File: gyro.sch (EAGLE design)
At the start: 12 parts, among them IC3 FXAS21002C

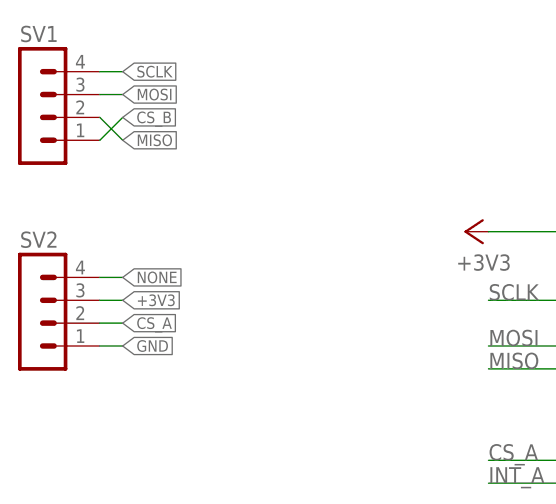
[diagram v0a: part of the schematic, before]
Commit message: INT_A i dopasowanie goldpinow
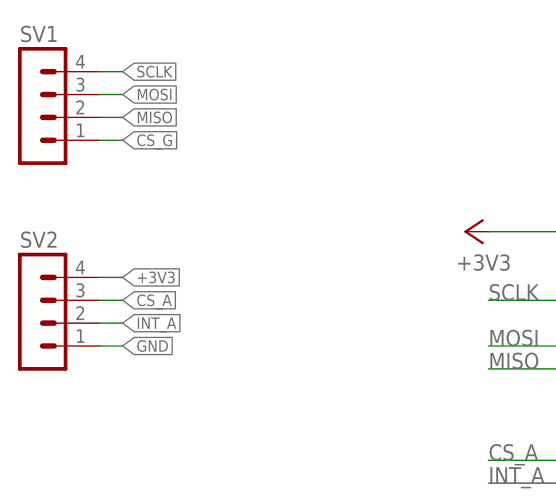
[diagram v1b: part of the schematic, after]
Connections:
- net CS_B renamed CS_G
- net N$28 renamed INT_G
- removed net NONE: SV2.4
- net +3V3: now also SV2.4; no longer SV2.3
- net CS_A: now also SV2.3; no longer SV2.2
- net INT_A: now also SV2.2
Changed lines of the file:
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@@
 <segment>
 <pinref part="SV1" gate="1" pin="2"/>
-<wire x1="-96.52" y1="60.96" x2="-93.98" y2="58.42" width="0.1524" layer="91"/>
-<label x="-93.98" y="58.42" size="1.27" layer="95" xref="yes"/>
+<wire x1="-96.52" y1="60.96" x2="-93.98" y2="60.96" width="0.1524" layer="91"/>
+<label x="-93.98" y="60.96" size="1.27" layer="95" xref="yes"/>
 </segment>
 </net>
@@
 <label x="-53.34" y="20.32" size="1.778" layer="95"/>
 </segment>
+<segment>
+<pinref part="SV2" gate="1" pin="2"/>
+<wire x1="-96.52" y1="38.1" x2="-93.98" y2="38.1" width="0.1524" layer="91"/>
+<label x="-93.98" y="38.1" size="1.27" layer="95" xref="yes"/>
+</segment>
 </net>
 <net name="+3V3" class="0">
@@
 </segment>
 <segment>
-<pinref part="SV2" gate="1" pin="3"/>
-<wire x1="-96.52" y1="40.64" x2="-93.98" y2="40.64" width="0.1524" layer="91"/>
-<label x="-93.98" y="40.64" size="1.27" layer="95" xref="yes"/>
+<pinref part="SV2" gate="1" pin="4"/>
+<wire x1="-96.52" y1="43.18" x2="-93.98" y2="43.18" width="0.1524" layer="91"/>
+<label x="-93.98" y="43.18" size="1.27" layer="95" xref="yes"/>
 </segment>
 <segment>
@@
 </segment>
 </net>
-<net name="CS_B" class="0">
-<segment>
-<pinref part="IC3" gate="G$1" pin="SPI_CS_B"/>
-<wire x1="17.78" y1="-30.48" x2="20.32" y2="-30.48" width="0.1524" layer="91"/>
-</segment>
-<segment>
-<pinref part="SV1" gate="1" pin="1"/>
-<wire x1="-96.52" y1="58.42" x2="-93.98" y2="60.96" width="0.1524" layer="91"/>
-<label x="-93.98" y="60.96" size="1.27" layer="95" xref="yes"/>
-</segment>
-</net>
 <net name="N$26" class="0">
 <segment>
@@
 </segment>
 </net>
-<net name="N$28" class="0">
-<segment>
-<pinref part="IC3" gate="G$1" pin="INT1"/>
-<wire x1="-22.86" y1="-30.48" x2="-25.4" y2="-30.48" width="0.1524" layer="91"/>
-</segment>
-</net>
 <net name="N$30" class="0">
 <segment>
@@
 </segment>
 </net>
-<net name="NONE" class="0">
+<net name="INT_G" class="0">
 <segment>
-<pinref part="SV2" gate="1" pin="4"/>
-<wire x1="-96.52" y1="43.18" x2="-93.98" y2="43.18" width="0.1524" layer="91"/>
-<label x="-93.98" y="43.18" size="1.27" layer="95" xref="yes"/>
+<pinref part="IC3" gate="G$1" pin="INT1"/>
+<wire x1="-22.86" y1="-30.48" x2="-25.4" y2="-30.48" width="0.1524" layer="91"/>
 </segment>
 </net>
@@
 </segment>
 <segment>
-<pinref part="SV2" gate="1" pin="2"/>
-<wire x1="-96.52" y1="38.1" x2="-93.98" y2="38.1" width="0.1524" layer="91"/>
-<label x="-93.98" y="38.1" size="1.27" layer="95" xref="yes"/>
+<pinref part="SV2" gate="1" pin="3"/>
+<wire x1="-96.52" y1="40.64" x2="-93.98" y2="40.64" width="0.1524" layer="91"/>
+<label x="-93.98" y="40.64" size="1.27" layer="95" xref="yes"/>
 </segment>
 </net>
+<net name="CS_G" class="0">
+<segment>
+<pinref part="IC3" gate="G$1" pin="SPI_CS_B"/>
+<wire x1="17.78" y1="-30.48" x2="20.32" y2="-30.48" width="0.1524" layer="91"/>
+</segment>
+<segment>
+<pinref part="SV1" gate="1" pin="1"/>
+<wire x1="-96.52" y1="58.42" x2="-93.98" y2="58.42" width="0.1524" layer="91"/>
+<label x="-93.98" y="58.42" size="1.27" layer="95" xref="yes"/>
+</segment>
+</net>

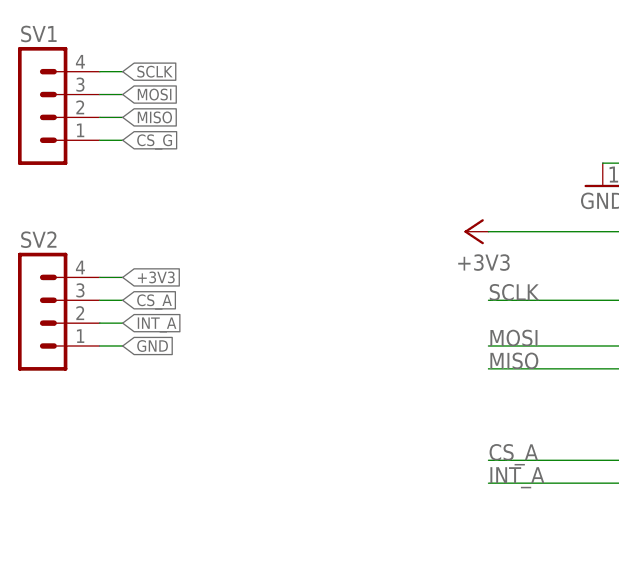
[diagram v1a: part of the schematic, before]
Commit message: dodanie wymiarowania do gyro i zepsucie termali :P
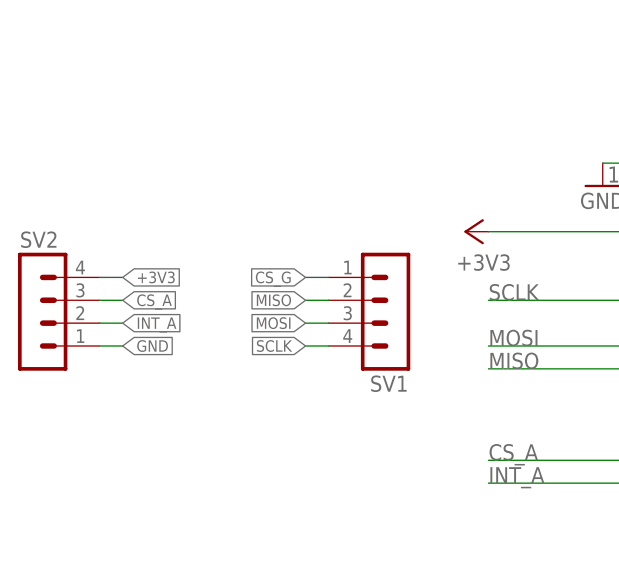
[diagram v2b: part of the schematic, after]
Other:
- moved on the sheet: SV1
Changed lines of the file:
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@@
 <instance part="C9" gate="G$1" x="30.48" y="-20.32"/>
 <instance part="C10" gate="G$1" x="35.56" y="-38.1"/>
-<instance part="SV1" gate="1" x="-104.14" y="63.5"/>
+<instance part="SV1" gate="1" x="-63.5" y="38.1" rot="R180"/>
 <instance part="SV2" gate="1" x="-104.14" y="40.64"/>
 <instance part="R1" gate="G$1" x="-43.18" y="-25.4" rot="R90"/>
@@
 <segment>
 <pinref part="SV1" gate="1" pin="3"/>
-<wire x1="-96.52" y1="63.5" x2="-93.98" y2="63.5" width="0.1524" layer="91"/>
-<label x="-93.98" y="63.5" size="1.27" layer="95" xref="yes"/>
+<wire x1="-71.12" y1="38.1" x2="-73.66" y2="38.1" width="0.1524" layer="91"/>
+<label x="-73.66" y="38.1" size="1.27" layer="95" rot="R180" xref="yes"/>
 </segment>
 </net>
@@
 <segment>
 <pinref part="SV1" gate="1" pin="2"/>
-<wire x1="-96.52" y1="60.96" x2="-93.98" y2="60.96" width="0.1524" layer="91"/>
-<label x="-93.98" y="60.96" size="1.27" layer="95" xref="yes"/>
+<wire x1="-71.12" y1="40.64" x2="-73.66" y2="40.64" width="0.1524" layer="91"/>
+<label x="-73.66" y="40.64" size="1.27" layer="95" rot="R180" xref="yes"/>
 </segment>
 </net>
@@
 <segment>
 <pinref part="SV1" gate="1" pin="4"/>
-<wire x1="-96.52" y1="66.04" x2="-93.98" y2="66.04" width="0.1524" layer="91"/>
-<label x="-93.98" y="66.04" size="1.27" layer="95" xref="yes"/>
+<wire x1="-71.12" y1="35.56" x2="-73.66" y2="35.56" width="0.1524" layer="91"/>
+<label x="-73.66" y="35.56" size="1.27" layer="95" rot="R180" xref="yes"/>
 </segment>
 </net>
@@
 <segment>
 <pinref part="SV1" gate="1" pin="1"/>
-<wire x1="-96.52" y1="58.42" x2="-93.98" y2="58.42" width="0.1524" layer="91"/>
-<label x="-93.98" y="58.42" size="1.27" layer="95" xref="yes"/>
-</segment>
-</net>
+<wire x1="-71.12" y1="43.18" x2="-73.66" y2="43.18" width="0.1524" layer="91"/>
+<label x="-73.66" y="43.18" size="1.27" layer="95" rot="R180" xref="yes"/>
+</segment>
+</net>

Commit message: gerbery do gyro
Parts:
- renumbered SV1 to SPI, SV2 to ZAS
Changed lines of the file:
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@@
 <part name="C9" library="rcl" deviceset="C-EU" device="C0603" value="100n"/>
 <part name="C10" library="rcl" deviceset="C-EU" device="C0603" value="100n"/>
-<part name="SV1" library="con-lstb" deviceset="MA04-1" device=""/>
-<part name="SV2" library="con-lstb" deviceset="MA04-1" device=""/>
+<part name="SPI" library="con-lstb" deviceset="MA04-1" device=""/>
+<part name="ZAS" library="con-lstb" deviceset="MA04-1" device=""/>
 <part name="R1" library="rcl" deviceset="R-EU_" device="R0603"/>
 <part name="+3V1" library="supply1" deviceset="+3V3" device=""/>
@@
 <instance part="C9" gate="G$1" x="30.48" y="-20.32"/>
 <instance part="C10" gate="G$1" x="35.56" y="-38.1"/>
-<instance part="SV1" gate="1" x="-63.5" y="38.1" rot="R180"/>
-<instance part="SV2" gate="1" x="-104.14" y="40.64"/>
+<instance part="SPI" gate="1" x="-63.5" y="38.1" rot="R180"/>
+<instance part="ZAS" gate="1" x="-104.14" y="40.64"/>
 <instance part="R1" gate="G$1" x="-43.18" y="-25.4" rot="R90"/>
 <instance part="+3V1" gate="G$1" x="-7.62" y="-60.96" rot="R180"/>
@@
 </segment>
 <segment>
-<pinref part="SV2" gate="1" pin="1"/>
+<pinref part="ZAS" gate="1" pin="1"/>
 <wire x1="-96.52" y1="35.56" x2="-93.98" y2="35.56" width="0.1524" layer="91"/>
 <label x="-93.98" y="35.56" size="1.27" layer="95" xref="yes"/>
@@
 </segment>
 <segment>
-<pinref part="SV1" gate="1" pin="3"/>
+<pinref part="SPI" gate="1" pin="3"/>
 <wire x1="-71.12" y1="38.1" x2="-73.66" y2="38.1" width="0.1524" layer="91"/>
 <label x="-73.66" y="38.1" size="1.27" layer="95" rot="R180" xref="yes"/>
@@
 </segment>
 <segment>
-<pinref part="SV1" gate="1" pin="2"/>
+<pinref part="SPI" gate="1" pin="2"/>
 <wire x1="-71.12" y1="40.64" x2="-73.66" y2="40.64" width="0.1524" layer="91"/>
 <label x="-73.66" y="40.64" size="1.27" layer="95" rot="R180" xref="yes"/>
@@
 </segment>
 <segment>
-<pinref part="SV1" gate="1" pin="4"/>
+<pinref part="SPI" gate="1" pin="4"/>
 <wire x1="-71.12" y1="35.56" x2="-73.66" y2="35.56" width="0.1524" layer="91"/>
 <label x="-73.66" y="35.56" size="1.27" layer="95" rot="R180" xref="yes"/>
@@
 </segment>
 <segment>
-<pinref part="SV2" gate="1" pin="2"/>
+<pinref part="ZAS" gate="1" pin="2"/>
 <wire x1="-96.52" y1="38.1" x2="-93.98" y2="38.1" width="0.1524" layer="91"/>
 <label x="-93.98" y="38.1" size="1.27" layer="95" xref="yes"/>
@@
 </segment>
 <segment>
-<pinref part="SV2" gate="1" pin="4"/>
+<pinref part="ZAS" gate="1" pin="4"/>
 <wire x1="-96.52" y1="43.18" x2="-93.98" y2="43.18" width="0.1524" layer="91"/>
 <label x="-93.98" y="43.18" size="1.27" layer="95" xref="yes"/>
@@
 </segment>
 <segment>
-<pinref part="SV2" gate="1" pin="3"/>
+<pinref part="ZAS" gate="1" pin="3"/>
 <wire x1="-96.52" y1="40.64" x2="-93.98" y2="40.64" width="0.1524" layer="91"/>
 <label x="-93.98" y="40.64" size="1.27" layer="95" xref="yes"/>
@@
 </segment>
 <segment>
-<pinref part="SV1" gate="1" pin="1"/>
+<pinref part="SPI" gate="1" pin="1"/>
 <wire x1="-71.12" y1="43.18" x2="-73.66" y2="43.18" width="0.1524" layer="91"/>
 <label x="-73.66" y="43.18" size="1.27" layer="95" rot="R180" xref="yes"/>

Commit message: poprawa bledow, dodanie rezystorow na wyjsciach stm-glownie w modolach, poprawa elementu 9axis z biblioteki
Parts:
- added INT_G: (no value), pinhead:PINHD-1X1
- added R2, R3, R4: (no value), rcl:R-EU_R0603
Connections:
- removed net INT_G: IC3.INT1
- new net N$1: R2.1, SPI.2
- new net N$2: INT_G.1, R3.2
- new net N$3: IC3.INT1, R3.1
- new net N$4: R4.2, ZAS.2
- net INT_A: now also R4.1; no longer ZAS.2
- net MISO: now also R2.2; no longer SPI.2
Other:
- moved on the sheet: ZAS
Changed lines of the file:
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@@
 <part name="R1" library="rcl" deviceset="R-EU_" device="R0603"/>
 <part name="+3V1" library="supply1" deviceset="+3V3" device=""/>
+<part name="INT_G" library="pinhead" deviceset="PINHD-1X1" device=""/>
+<part name="R2" library="rcl" deviceset="R-EU_" device="R0603"/>
+<part name="R3" library="rcl" deviceset="R-EU_" device="R0603"/>
+<part name="R4" library="rcl" deviceset="R-EU_" device="R0603"/>
 </parts>
 <sheets>
@@
 <instance part="C10" gate="G$1" x="35.56" y="-38.1"/>
 <instance part="SPI" gate="1" x="-63.5" y="38.1" rot="R180"/>
-<instance part="ZAS" gate="1" x="-104.14" y="40.64"/>
+<instance part="ZAS" gate="1" x="-116.84" y="40.64"/>
 <instance part="R1" gate="G$1" x="-43.18" y="-25.4" rot="R90"/>
 <instance part="+3V1" gate="G$1" x="-7.62" y="-60.96" rot="R180"/>
+<instance part="INT_G" gate="G$1" x="-66.04" y="-30.48" rot="R180"/>
+<instance part="R2" gate="G$1" x="-76.2" y="40.64" rot="R180"/>
+<instance part="R3" gate="G$1" x="-53.34" y="-30.48" rot="R180"/>
+<instance part="R4" gate="G$1" x="-104.14" y="38.1" rot="R180"/>
 </instances>
 <busses>
@@
 <segment>
 <pinref part="ZAS" gate="1" pin="1"/>
-<wire x1="-96.52" y1="35.56" x2="-93.98" y2="35.56" width="0.1524" layer="91"/>
-<label x="-93.98" y="35.56" size="1.27" layer="95" xref="yes"/>
+<wire x1="-109.22" y1="35.56" x2="-106.68" y2="35.56" width="0.1524" layer="91"/>
+<label x="-106.68" y="35.56" size="1.27" layer="95" xref="yes"/>
 </segment>
 <segment>
@@
 </segment>
 <segment>
-<pinref part="SPI" gate="1" pin="2"/>
-<wire x1="-71.12" y1="40.64" x2="-73.66" y2="40.64" width="0.1524" layer="91"/>
-<label x="-73.66" y="40.64" size="1.27" layer="95" rot="R180" xref="yes"/>
+<pinref part="R2" gate="G$1" pin="2"/>
+<wire x1="-81.28" y1="40.64" x2="-83.82" y2="40.64" width="0.1524" layer="91"/>
+<label x="-83.82" y="40.64" size="1.27" layer="95" rot="R180" xref="yes"/>
 </segment>
 </net>
@@
 </segment>
 <segment>
-<pinref part="ZAS" gate="1" pin="2"/>
-<wire x1="-96.52" y1="38.1" x2="-93.98" y2="38.1" width="0.1524" layer="91"/>
-<label x="-93.98" y="38.1" size="1.27" layer="95" xref="yes"/>
+<pinref part="R4" gate="G$1" pin="1"/>
+<wire x1="-99.06" y1="38.1" x2="-96.52" y2="38.1" width="0.1524" layer="91"/>
+<label x="-96.52" y="38.1" size="1.27" layer="95" xref="yes"/>
 </segment>
 </net>
@@
 <segment>
 <pinref part="ZAS" gate="1" pin="4"/>
-<wire x1="-96.52" y1="43.18" x2="-93.98" y2="43.18" width="0.1524" layer="91"/>
-<label x="-93.98" y="43.18" size="1.27" layer="95" xref="yes"/>
+<wire x1="-109.22" y1="43.18" x2="-106.68" y2="43.18" width="0.1524" layer="91"/>
+<label x="-106.68" y="43.18" size="1.27" layer="95" xref="yes"/>
 </segment>
 <segment>
@@
 </segment>
 </net>
-<net name="INT_G" class="0">
-<segment>
-<pinref part="IC3" gate="G$1" pin="INT1"/>
-<wire x1="-22.86" y1="-30.48" x2="-25.4" y2="-30.48" width="0.1524" layer="91"/>
-</segment>
-</net>
 <net name="CS_A" class="0">
 <segment>
@@
 <segment>
 <pinref part="ZAS" gate="1" pin="3"/>
-<wire x1="-96.52" y1="40.64" x2="-93.98" y2="40.64" width="0.1524" layer="91"/>
-<label x="-93.98" y="40.64" size="1.27" layer="95" xref="yes"/>
+<wire x1="-109.22" y1="40.64" x2="-106.68" y2="40.64" width="0.1524" layer="91"/>
+<label x="-106.68" y="40.64" size="1.27" layer="95" xref="yes"/>
 </segment>
 </net>
@@
 </segment>
 </net>
+<net name="N$1" class="0">
+<segment>
+<pinref part="SPI" gate="1" pin="2"/>
+<pinref part="R2" gate="G$1" pin="1"/>
+</segment>
+</net>
+<net name="N$2" class="0">
+<segment>
+<pinref part="INT_G" gate="G$1" pin="1"/>
+<pinref part="R3" gate="G$1" pin="2"/>
+<wire x1="-63.5" y1="-30.48" x2="-58.42" y2="-30.48" width="0.1524" layer="91"/>
+</segment>
+</net>
+<net name="N$3" class="0">
+<segment>
+<pinref part="R3" gate="G$1" pin="1"/>
+<pinref part="IC3" gate="G$1" pin="INT1"/>
+<wire x1="-48.26" y1="-30.48" x2="-22.86" y2="-30.48" width="0.1524" layer="91"/>
+</segment>
+</net>
+<net name="N$4" class="0">
+<segment>
+<pinref part="ZAS" gate="1" pin="2"/>
+<pinref part="R4" gate="G$1" pin="2"/>
+</segment>
+</net>
